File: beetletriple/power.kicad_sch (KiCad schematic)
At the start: 20 parts, among them U1 TPS54331DR, U2 HT7550-1

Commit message: misc updates
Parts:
- removed C5: 220uF, Capacitor_SMD:C_Elec_10x10.2, symbol Device:C_Polarized
- added C5: 220uF, Capacitor_SMD:C_Elec_10x10.2, symbol Device:CP
- C3, C4: symbol Device:C_Polarized -> Device:CP
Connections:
- net GND: now also C5.2
- net VBEC: now also C5.1
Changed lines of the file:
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@@
   (junction (at 210.185 60.96) (diameter 0.9144) (color 0 0 0 0))
   (junction (at 210.185 80.01) (diameter 0.9144) (color 0 0 0 0))
-  (junction (at 235.585 60.96) (diameter 0.9144) (color 0 0 0 0))
+  (junction (at 224.155 60.96) (diameter 0.9144) (color 0 0 0 0))
+  (junction (at 224.155 62.23) (diameter 0.9144) (color 0 0 0 0))
+  (junction (at 227.965 60.96) (diameter 0.9144) (color 0 0 0 0))
   (junction (at 243.205 70.485) (diameter 0.9144) (color 0 0 0 0))
   (junction (at 250.19 60.96) (diameter 0.9144) (color 0 0 0 0))
@@
     (stroke (width 0) (type solid) (color 0 0 0 0))
   )
-  (wire (pts (xy 43.18 38.735) (xy 51.435 38.735))
-    (stroke (width 0) (type solid) (color 0 0 0 0))
-  )
   (wire (pts (xy 43.18 59.055) (xy 57.15 59.055))
     (stroke (width 0) (type solid) (color 0 0 0 0))
@@
     (stroke (width 0) (type solid) (color 0 0 0 0))
   )
+  (wire (pts (xy 51.435 38.735) (xy 43.18 38.735))
+    (stroke (width 0) (type solid) (color 0 0 0 0))
+  )
   (wire (pts (xy 51.435 38.735) (xy 70.485 38.735))
     (stroke (width 0) (type solid) (color 0 0 0 0))
@@
     (stroke (width 0) (type solid) (color 0 0 0 0))
   )
-  (wire (pts (xy 70.485 46.355) (xy 74.295 46.355))
+  (wire (pts (xy 74.295 46.355) (xy 70.485 46.355))
     (stroke (width 0) (type solid) (color 0 0 0 0))
   )
@@
     (stroke (width 0) (type solid) (color 0 0 0 0))
   )
-  (wire (pts (xy 168.275 62.23) (xy 168.275 68.58))
-    (stroke (width 0) (type solid) (color 0 0 0 0))
-  )
   (wire (pts (xy 168.275 62.23) (xy 168.91 62.23))
     (stroke (width 0) (type solid) (color 0 0 0 0))
   )
+  (wire (pts (xy 168.275 68.58) (xy 168.275 62.23))
+    (stroke (width 0) (type solid) (color 0 0 0 0))
+  )
   (wire (pts (xy 168.275 74.295) (xy 168.275 68.58))
     (stroke (width 0) (type solid) (color 0 0 0 0))
@@
     (stroke (width 0) (type solid) (color 0 0 0 0))
   )
-  (wire (pts (xy 184.785 60.96) (xy 193.675 60.96))
-    (stroke (width 0) (type solid) (color 0 0 0 0))
-  )
   (wire (pts (xy 184.785 68.58) (xy 168.275 68.58))
     (stroke (width 0) (type solid) (color 0 0 0 0))
@@
     (stroke (width 0) (type solid) (color 0 0 0 0))
   )
+  (wire (pts (xy 193.675 60.96) (xy 184.785 60.96))
+    (stroke (width 0) (type solid) (color 0 0 0 0))
+  )
   (wire (pts (xy 193.675 60.96) (xy 194.31 60.96))
     (stroke (width 0) (type solid) (color 0 0 0 0))
@@
     (stroke (width 0) (type solid) (color 0 0 0 0))
   )
-  (wire (pts (xy 210.185 60.96) (xy 235.585 60.96))
+  (wire (pts (xy 210.185 60.96) (xy 250.19 60.96))
     (stroke (width 0) (type solid) (color 0 0 0 0))
   )
@@
     (stroke (width 0) (type solid) (color 0 0 0 0))
   )
-  (wire (pts (xy 235.585 60.96) (xy 250.19 60.96))
-    (stroke (width 0) (type solid) (color 0 0 0 0))
-  )
-  (wire (pts (xy 235.585 68.58) (xy 235.585 70.485))
-    (stroke (width 0) (type solid) (color 0 0 0 0))
-  )
-  (wire (pts (xy 235.585 70.485) (xy 243.205 70.485))
+  (wire (pts (xy 224.155 60.96) (xy 224.155 62.23))
+    (stroke (width 0) (type solid) (color 0 0 0 0))
+  )
+  (wire (pts (xy 224.155 62.23) (xy 224.155 62.865))
+    (stroke (width 0) (type solid) (color 0 0 0 0))
+  )
+  (wire (pts (xy 224.155 62.23) (xy 227.965 62.23))
+    (stroke (width 0) (type solid) (color 0 0 0 0))
+  )
+  (wire (pts (xy 224.155 70.485) (xy 243.205 70.485))
+    (stroke (width 0) (type solid) (color 0 0 0 0))
+  )
+  (wire (pts (xy 227.965 60.96) (xy 227.965 62.23))
     (stroke (width 0) (type solid) (color 0 0 0 0))
   )
@@
   (symbol (lib_id "power:PWR_FLAG") (at 74.295 46.355 180) (unit 1)
     (in_bom yes) (on_board yes)
-    (property "Reference" "#FLG?" (id 0) (at 74.295 48.26 0)
+    (property "Reference" "#FLG01" (id 0) (at 74.295 48.26 0)
       (effects (font (size 1.27 1.27)) hide)
     )
@@
     (pin "2")
   )
-  (symbol (lib_id "Device:C_Polarized") (at 43.18 62.865 0) (unit 1)
+  (symbol (lib_id "Device:CP") (at 43.18 62.865 0) (unit 1)
     (in_bom yes) (on_board yes)
     (property "Reference" "C3" (id 0) (at 46.1011 61.7156 0)
@@
     (pin "2")
   )
-  (symbol (lib_id "Device:C_Polarized") (at 57.15 62.865 0) (unit 1)
+  (symbol (lib_id "Device:CP") (at 57.15 62.865 0) (unit 1)
     (in_bom yes) (on_board yes)
     (property "Reference" "C4" (id 0) (at 60.0711 61.7156 0)
@@
     (pin "2")
   )
-  (symbol (lib_id "Device:C_Polarized") (at 235.585 64.77 0) (unit 1)
-    (in_bom yes) (on_board yes)
-    (property "Reference" "C5" (id 0) (at 238.5061 63.6206 0)
-      (effects (font (size 1.27 1.27)) (justify left))
-    )
-    (property "Value" "220uF" (id 1) (at 238.506 65.919 0)
-      (effects (font (size 1.27 1.27)) (justify left))
-    )
-    (property "Footprint" "Capacitor_SMD:C_Elec_10x10.2" (id 2) (at 236.5502 68.58 0)
-      (effects (font (size 1.27 1.27)) hide)
-    )
-    (property "Datasheet" "~" (id 3) (at 235.585 64.77 0)
-      (effects (font (size 1.27 1.27)) hide)
-    )
-    (property "LCSC" "C125977" (id 4) (at 235.585 64.77 0)
-      (effects (font (size 1.27 1.27)) hide)
-    )
+  (symbol (lib_id "Device:CP") (at 224.155 66.675 0) (unit 1)
+    (in_bom yes) (on_board yes)
+    (property "Reference" "C5" (id 0) (at 227.076 65.526 0)
+      (effects (font (size 1.27 1.27)) (justify left))
+    )
+    (property "Value" "220uF" (id 1) (at 227.076 67.824 0)
+      (effects (font (size 1.27 1.27)) (justify left))
+    )
+    (property "Footprint" "Capacitor_SMD:C_Elec_10x10.2" (id 2) (at 225.1202 70.485 0)
+      (effects (font (size 1.27 1.27)) hide)
+    )
+    (property "Datasheet" "~" (id 3) (at 224.155 66.675 0)
+      (effects (font (size 1.27 1.27)) hide)
+    )
+    (property "LCSC" "C125977" (id 4) (at 224.155 66.675 0)
+      (effects (font (size 1.27 1.27)) hide)
+    )

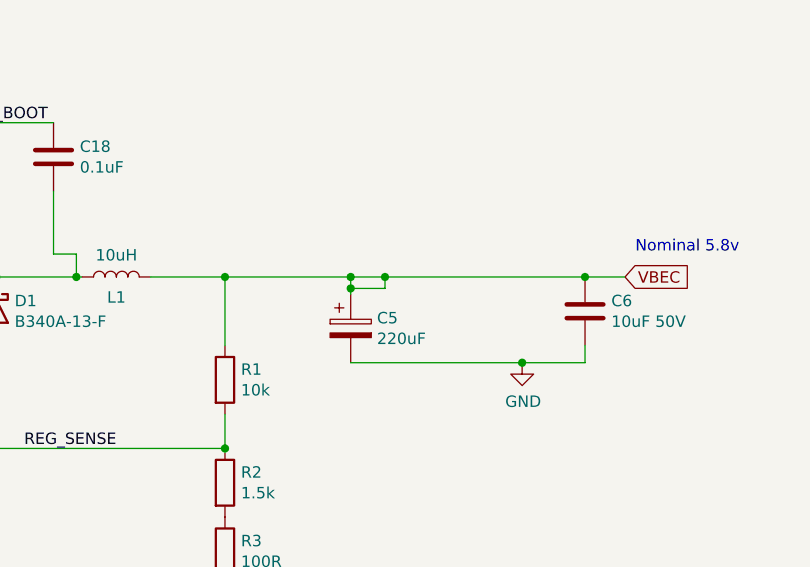
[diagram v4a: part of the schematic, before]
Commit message: Shunt current sensor. Many improvements, layout updates
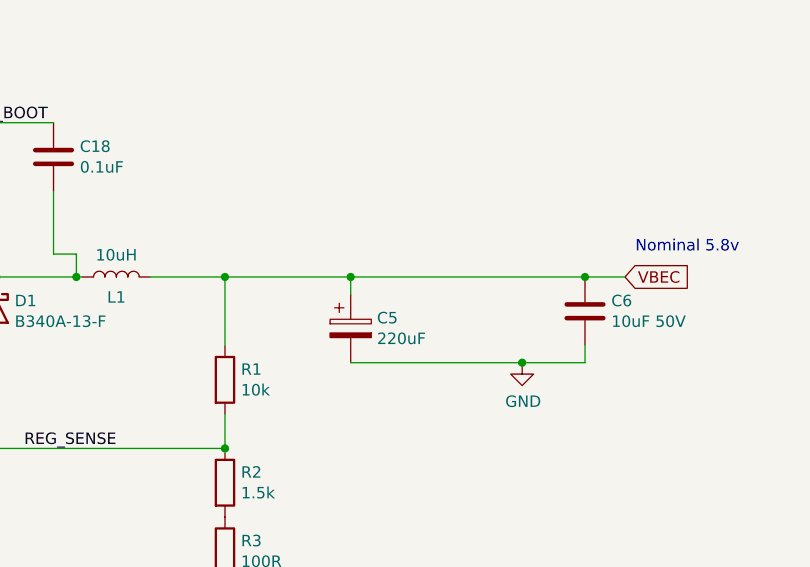
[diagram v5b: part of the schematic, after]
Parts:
- F1: footprint Fuse:Fuseholder_Cylinder-5x20mm_Schurter_0031_8201_Horizontal_Open -> beetletriple:fuseholder_flexible
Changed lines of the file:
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@@
   (junction (at 210.185 80.01) (diameter 0.9144) (color 0 0 0 0))
   (junction (at 224.155 60.96) (diameter 0.9144) (color 0 0 0 0))
-  (junction (at 224.155 62.23) (diameter 0.9144) (color 0 0 0 0))
-  (junction (at 227.965 60.96) (diameter 0.9144) (color 0 0 0 0))
   (junction (at 243.205 70.485) (diameter 0.9144) (color 0 0 0 0))
   (junction (at 250.19 60.96) (diameter 0.9144) (color 0 0 0 0))
@@
     (stroke (width 0) (type solid) (color 0 0 0 0))
   )
-  (wire (pts (xy 210.185 60.96) (xy 250.19 60.96))
+  (wire (pts (xy 210.185 60.96) (xy 224.155 60.96))
     (stroke (width 0) (type solid) (color 0 0 0 0))
   )
@@
     (stroke (width 0) (type solid) (color 0 0 0 0))
   )
-  (wire (pts (xy 224.155 60.96) (xy 224.155 62.23))
-    (stroke (width 0) (type solid) (color 0 0 0 0))
-  )
-  (wire (pts (xy 224.155 62.23) (xy 224.155 62.865))
-    (stroke (width 0) (type solid) (color 0 0 0 0))
-  )
-  (wire (pts (xy 224.155 62.23) (xy 227.965 62.23))
+  (wire (pts (xy 224.155 60.96) (xy 224.155 62.865))
+    (stroke (width 0) (type solid) (color 0 0 0 0))
+  )
+  (wire (pts (xy 224.155 60.96) (xy 250.19 60.96))
     (stroke (width 0) (type solid) (color 0 0 0 0))
   )
   (wire (pts (xy 224.155 70.485) (xy 243.205 70.485))
-    (stroke (width 0) (type solid) (color 0 0 0 0))
-  )
-  (wire (pts (xy 227.965 60.96) (xy 227.965 62.23))
     (stroke (width 0) (type solid) (color 0 0 0 0))
   )
@@
     (property "Reference" "F1" (id 0) (at 36.83 33.7628 90))
     (property "Value" "20mmx5 fuse holder" (id 1) (at 36.83 36.061 90))
-    (property "Footprint" "Fuse:Fuseholder_Cylinder-5x20mm_Schurter_0031_8201_Horizontal_Open" (id 2) (at 36.83 40.513 90)
-      (effects (font (size 1.27 1.27)) hide)
-    )
+    (property "Footprint" "beetletriple:fuseholder_flexible" (id 2) (at 36.83 40.513 90)
+      (effects (font (size 1.27 1.27)) hide)
+    )

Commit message: add lcsc part numbers
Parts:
- C17: LCSC (none) -> C1846
- C18: LCSC (none) -> C24497
- D1: MPN (none) -> B340A
- L1: LCSC (none) -> C497890
- R1: LCSC (none) -> C17414
- R2: LCSC (none) -> C4310
- R3: LCSC (none) -> C17408
- U1: LCSC (none) -> C9865
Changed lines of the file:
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@@
       (effects (font (size 1.27 1.27)) hide)
     )
-    (property "LCSC" "" (id 4) (at 198.12 60.96 90)
+    (property "LCSC" "C497890" (id 4) (at 198.12 60.96 90)
       (effects (font (size 1.27 1.27)) hide)
     )
@@
       (effects (font (size 1.27 1.27)) hide)
     )
+    (property "LCSC" "C17414" (id 4) (at 210.185 72.39 0)
+      (effects (font (size 1.27 1.27)) hide)
+    )
     (pin "1")
     (pin "2")
@@
       (effects (font (size 1.27 1.27)) hide)
     )
+    (property "LCSC" "C4310" (id 4) (at 210.185 83.82 0)
+      (effects (font (size 1.27 1.27)) hide)
+    )
     (pin "1")
     (pin "2")
@@
       (effects (font (size 1.27 1.27)) hide)
     )
+    (property "LCSC" "C17408" (id 4) (at 210.185 91.44 0)
+      (effects (font (size 1.27 1.27)) hide)
+    )
     (pin "1")
     (pin "2")
@@
       (effects (font (size 1.27 1.27)) hide)
     )
+    (property "MPN" "B340A" (id 4) (at 184.785 64.77 0)
+      (effects (font (size 1.27 1.27)) hide)
+    )
     (pin "1")
     (pin "2")
@@
       (effects (font (size 1.27 1.27)) hide)
     )
+    (property "LCSC" "C1846" (id 4) (at 135.255 55.245 0)
+      (effects (font (size 1.27 1.27)) hide)
+    )
     (pin "1")
     (pin "2")
@@
     )
     (property "Datasheet" "~" (id 3) (at 191.135 47.625 0)
+      (effects (font (size 1.27 1.27)) hide)
+    )
+    (property "LCSC" "C24497" (id 4) (at 191.135 47.625 0)
       (effects (font (size 1.27 1.27)) hide)
     )
@@
       (effects (font (size 1.27 1.27)) hide)
     )
+    (property "LCSC" "C9865" (id 4) (at 168.91 48.895 0)
+      (effects (font (size 1.27 1.27)) hide)
+    )
